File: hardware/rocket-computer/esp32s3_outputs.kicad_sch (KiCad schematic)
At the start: 40 parts, among them J5 Conn_01x04, SW3 R-667995, U11 GD5F2GQ5UEYIGR, U13 GD25Q128ESIG, U14 479480001, U15 ESP32-S3RH2, U29 TPS22810DRVR, Y1 ABS07-32.768KHZ-T, Y2 ECS-400-10-37B2-CKY-TR

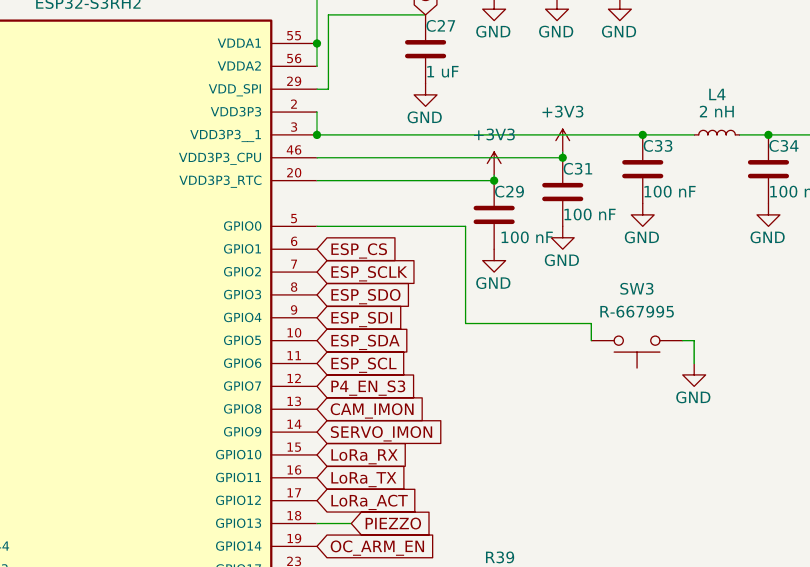
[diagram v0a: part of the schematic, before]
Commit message: hardware: I2S net names on both rocket computers; FC LED map and GPIO47/48 fixes (#987)
Renames the four inter-MCU link nets on both rocket computers to say what they
are — the link is I2S plus a sideband GPIO, and the names read as SPI:
ESP_SCLK -> ESP_I2S_BCLK, ESP_CS -> ESP_I2S_WS, ESP_SDO -> ESP_I2S_SD,
ESP_SDI -> ESP_I2S_FSYNC. ESP_SCL/ESP_SDA keep their names. ESP_I2S_FSYNC is not
a peripheral signal: the master pulses it around each writeFrame() and the slave
reads it to resync. Boards fabbed before this carry the old labels; the GPIO
numbers are unchanged and board_v9.h records both.

Also fixes three defects a header-vs-netlist parity sweep found on the mini:

- BMP585_CS and ISM6HG256_INT were swapped on both mini headers. ESP-IDF pins
  GPIO47 = SPICLK_P and GPIO48 = SPICLK_N; the schematic puts BMP585_CS on pad
  36 (SPICLK_N) and ISM6HG256_INT1 on pad 37 (SPICLK_P), so the correct numbers
  are 48 and 47. As shipped the barometer chip select would never have asserted
  and the IMU interrupt line would have been driven as an output.
- The flight computer has two LEDs, not one: IND_1 -> R70 -> D10 red on GPIO38
  and IND_2 -> R71 -> D11 blue on GPIO45. board_m1.h named the blue one red,
  left the red one unclaimed, and cited parts that do not exist. main.cpp drives
  BLUE_LED_PIN with no >= 0 guard, so the mini passed (gpio_num_t)-1 every boot.
- Docs corrected for FC GPIO3 (it carries VBUCK_OK through the R137/R138
  divider) and for the flight computer's spare pads (GPIO43 alone).

Includes the mini layout pass: 214 footprints placed, the 22.5 x 69.5 mm outline
restored on Edge.Cuts, and the board re-synced from the schematic. It is placed
but not routed. Before that re-sync the board file lagged the schematic by two
reworks and kicad-cli pcb drc --schematic-parity did not flag it, because it
reconciles footprints rather than stale net strings.

Verified: netlist fingerprints diff to exactly the four renames with identical
node lists on both boards; co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
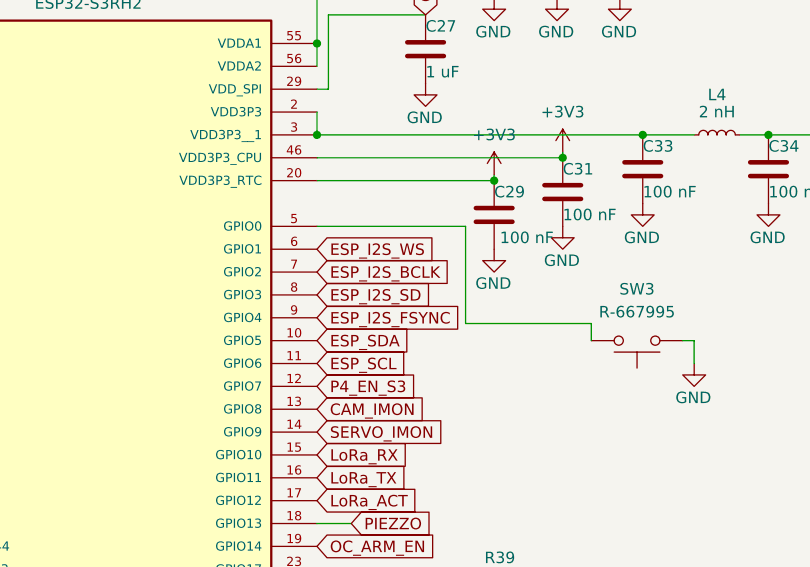
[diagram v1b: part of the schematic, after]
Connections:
- net ESP_CS renamed ESP_I2S_WS
- net ESP_SCLK renamed ESP_I2S_BCLK
- net ESP_SDI renamed ESP_I2S_FSYNC
- net ESP_SDO renamed ESP_I2S_SD
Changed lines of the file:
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@@
 		)
 	)
-	(global_label "ESP_CS"
+	(global_label "ESP_I2S_WS"
 		(shape input)
 		(at 212.725 53.34 0)
@@
 		)
 	)
-	(global_label "ESP_SCLK"
+	(global_label "ESP_I2S_BCLK"
 		(shape input)
 		(at 212.725 55.88 0)
@@
 		)
 	)
-	(global_label "ESP_SDO"
+	(global_label "ESP_I2S_SD"
 		(shape input)
 		(at 212.725 58.42 0)
@@
 		)
 	)
-	(global_label "ESP_SDI"
+	(global_label "ESP_I2S_FSYNC"
 		(shape input)
 		(at 212.725 60.96 0)

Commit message: hardware(V10): close out #664, #665 and #677 — the VDD_SPI 100 nF, the CHIP_PU rail-cycle analysis, and the harness cable rule (#1357)
Three items from the V9 pre-fab review list whose electrical content had
already landed; this closes what each still owed.

## #664 — C145 100 nF on OUT_VDD_SPI

The S3's VDD_SPI pin serves only the in-package PSRAM (the boot flash and
the NAND run from +3V3) and carried C27 1 uF alone; the design guide asks
for 1 uF + 0.1 uF at the pin and there was no pad for the second part.
C145 is drawn beside C27 on the same wire, split at (219.71, 27.305) with a
junction. Netlist: OUT_VDD_SPI = {C145.1, C27.1, U15.29}; C145.2 = GND.
bom.csv: 261 designators, 0 mismatches. WORKLIST M-4 and power-eco.md
Change 6 record the close-out. Placement at U15 pin 29 is the layout
pass's.

## #665 — CHIP_PU through a rail cycle

Both reset RCs are in copper on V9. The residual (the P4's C39 bleeding
into the QOD-collapsed rail at tau = 10 ms, so a rail re-raised inside
~14 ms would ramp with CHIP_PU high) is analysed in
v10-power-parity-2026-09-11.md section 6.2: the window is a coincidence
between C105's 0.45-0.94 s hold and the out computer's re-assert instant,
the pad clamp very likely collapses the node with the rail (inferred, not
specified), and a boot that misses t_STBL costs one extra rail cycle
because a P4 that never asserts P4_EN_HOLD gets its rail re-cycled by the
restore policy. The scope check that settles it is now on #1211. No part
change; the 100 nF that would shorten the window is the delay the design
guide asks for.

## #677 — mis-connection protection

Reverse battery is closed by Q11 with CR2 deleted; the PH-2-into-PH-4
mismate cannot happen since the battery moved to a JST-VH; the reversed
jumper is closed as a harness rule. New hardware/cables.md records the
straight "A"-suffix jumper part numbers (A04SR04SR30K51A, A05SR05SR30K51A),
the Digi-Key "Reversed" naming trap that cooked a radio on 2026-07-31, the
pad-1-to-pad-1 check, and 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
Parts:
- added C145: 100 nF, Capacitor_SMD:C_0402_1005Metric, symbol Device:C
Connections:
- net GND: now also C145.2
- net OUT_VDD_SPI: now also C145.1
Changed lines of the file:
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@@
 	(wire
 		(pts
-			(xy 213.995 27.305) (xy 224.79 27.305)
+			(xy 213.995 27.305) (xy 219.71 27.305)
 		)
 		(stroke
@@
 	(wire
 		(pts
+			(xy 219.71 27.305) (xy 224.79 27.305)
+		)
+		(stroke
+			(width 0)
+			(type default)
+		)
+	)
+	(junction
+		(at 219.71 27.305)
+		(diameter 0)
+		(color 0 0 0 0)
+	)
+	(wire
+		(pts
 			(xy 154.94 35.56) (xy 154.94 36.83)
 		)
@@
 			)
 		)
+	)
+	(symbol
+		(lib_id "Device:C")
+		(at 219.71 31.115 0)
+		(unit 1)
+		(body_style 1)
+		(exclude_from_sim no)
+		(in_bom yes)
+		(on_board yes)
+		(in_pos_files yes)
+		(dnp no)
+		(property "Reference" "C145"
+			(at 219.71 22.86 0)
+			(show_name no)
+			(do_not_autoplace no)
+			(effects
+				(font
+					(size 1.27 1.27)
+				)
+				(justify right)
+			)
+		)
+		(property "Value" "100 nF"
+			(at 219.71 25.4 0)
+			(show_name no)
+			(do_not_autoplace no)
+			(effects
+				(font
+					(size 1.27 1.27)
+				)
+				(justify right)
+			)
+		)
+		(property "Footprint" "Capacitor_SMD:C_0402_1005Metric"
+			(at 219.71 34.925 0)
+			(hide yes)
+			(show_name no)
+			(do_not_autoplace no)
+			(effects
+				(font
+					(size 1.27 1.27)
+				)
+			)
+		)
+		(property "Datasheet" ""
+			(at 219.71 31.115 0)
+			(hide yes)
+			(show_name no)
+			(do_not_autoplace no)
+			(effects
+				(font
+					(size 1.27 1.27)
+				)
+			)
+		)
+		(property "Description" "Unpolarized capacitor"
+			(at 219.71 31.115 0)
+			(hide yes)
+			(show_name no)
+			(do_not_autoplace no)
+			(effects
+				(font
+					(size 1.27 1.27)
+				)
+			)
+		)
+		(property "MPN" "CL05B104KO5NNNC"
+			(at 219.71 31.115 0)
+			(hide yes)
+			(show_name no)
+			(do_not_autoplace no)
+			(effects
+				(font
+					(size 1.27 1.27)
+				)
+			)
+		)
+		(property "Mfr" "Samsung"
+			(at 219.71 31.115 0)
+			(hide yes)
+			(show_name no)
+			(do_not_autoplace no)
+			(effects
+				(font
+					(size 1.27 1.27)
+				)
+			)
+		)
+		(pin "1"
+		)
+		(pin "2"
+		)
+		(instances
+			(project "rocket-computer"
+				(path "/ae61c2c4-72e9-4776-93ae-2e716b9dc70f/eab70588-b031-4461-adac-e038e88381cb"
+					(reference "C145")
+					(unit 1)
+				)
+			)
+		)
+	)
+	(symbol
+		(lib_id "power:GND")
+		(at 219.71 34.925 0)
+		(unit 1)
+		(body_style 1)
+		(exclude_from_sim no)
+		(in_bom yes)
+		(on_board yes)
+		(in_pos_files yes)
+		(dnp no)
+		(property "Reference" "#PWR0704"
+			(at 219.71 41.275 0)
+			(hide yes)
+			(show_name no)
+			(do_not_autoplace no)
+			(effects
+				(font
+					(size 1.27 1.27)
+				)
+			)
+		)
+		(property "Value" "GND"
+			(at 221.615 38.735 0)
+			(show_name no)
+			(do_not_autoplace no)
+			(effects
+				(font
+					(size 1.27 1.27)
+				)
+				(justify right)
+			)
+		)
+		(property "Footprint" ""
+			(at 219.71 34.925 0)
+			(hide yes)
+			(show_name no)
+			(do_not_autoplace no)
+			(effects
+				(font
+					(size 1.27 1.27)
+				)
+			)
+		)
+		(property "Datasheet" ""
+			(at 219.71 34.925 0)
+			(hide yes)
+			(show_name no)
+			(do_not_autoplace no)
+			(effects
+				(font
+					(size 1.27 1.27)
+				)
+			)
+		)
+		(property "Description" "Power symbol creates a global label with name \"GND\" , ground"
+			(at 219.71 34.925 0)
+			(hide yes)
+			(show_name no)
+			(do_not_autoplace no)
+			(effects
+				(font
+					(size 1.27 1.27)
+				)
+			)
+		)
+		(pin "1"
+		)
+		(instances
+			(project "rocket-computer"
+				(path "/ae61c2c4-72e9-4776-93ae-2e716b9dc70f/eab70588-b031-4461-adac-e038e88381cb"
+					(reference "#PWR0704")
+					(unit 1)
+				)
+			)
+		)

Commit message: hardware(V10): the #678 sweep — NRETRY to ground, LEDs at 1 k, H2 grounded, the missing bypasses, and the U9 pin-9 parity fix (#1360)
Schematic, library and BOM only; the board is untouched. Record:
hardware/rocket-computer/v10-power-parity-2026-09-11.md section 6.4.

## Owner decisions (2026-09-11)

- NRETRY to ground: C45 (1 uF, ~1800 retries, past the datasheet's last
  quantization bucket) deleted, U19 pin 11 tied to GND. With C46 2.2 nF
  still on RETRY_DLY the TPS25982 fault table reads "auto-retry
  indefinitely with finite delay" -- a finite count ends in latch-off,
  which a flight computer must never do.
- Status LEDs: R65, R66, R70 10 k -> 1 k (stocked line). ~1.5 mA green,
  ~1.3 mA red, ~0.4 mA blue instead of 0.05-0.15 mA.
- H2, the plated mounting ring 0.6 mm from the antenna body, on no net:
  H2 becomes Mechanical:MountingHole_Pad with pin 1 on GND. The other
  seven holes are unchanged; the pad's zone connection is the layout
  pass's.

## Simple adds from the same list

- C44 soft-start 390 pF -> 10 nF (the buck started in current limit into
  its output capacitance; ~5 ms now, datasheet class).
- R141 10 k pull-up on S3 GPIO0 to +3V3, on the wire to the boot button.
- C146 / C147 100 nF at the IMU and baro VDD pins (their nearest 100 nF
  was the magnetometer's at 3-4 mm), on V_MCU_SWTCH.
- C148 10 uF on the S3 RF supply net, converter side of L4 (the guide
  asks 10 uF per RF pin; there was only C33 100 nF).
- ISM6HG256_INT2: single-pin label replaced by a no-connect flag.
- U9 CSD16323Q3 symbol pin 9 renumbered 5 in Custom.kicad_sym and in the
  cached copies on this board and the mini: the shared TSON footprint
  numbers its drain tab as a second pad 5, so the symbol now matches it
  and the permanent "no pad for pin 9" parity warning is gone on both
  boards. Netlists unchanged.
- power-eco.md Change 2 pin table rewritten to the as-built designators
  and values (ITIMER/dVdt/NRETRY had drifted; the input clamp is gone).

Not changed, recorded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
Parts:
- added C148: 10 uF, Capacitor_SMD:C_0402_1005Metric, symbol Device:C
- added R141: 10 k, Resistor_SMD:R_0402_1005Metric, symbol Device:R_US
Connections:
- net +3V3: now also R141.2
- net GND: now also C148.2
- net at C33.1, L4.1, U15.2 (VDD3P3)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: now also C148.1
- net at SW3.2, U15.5 (GPIO0): now also R141.1

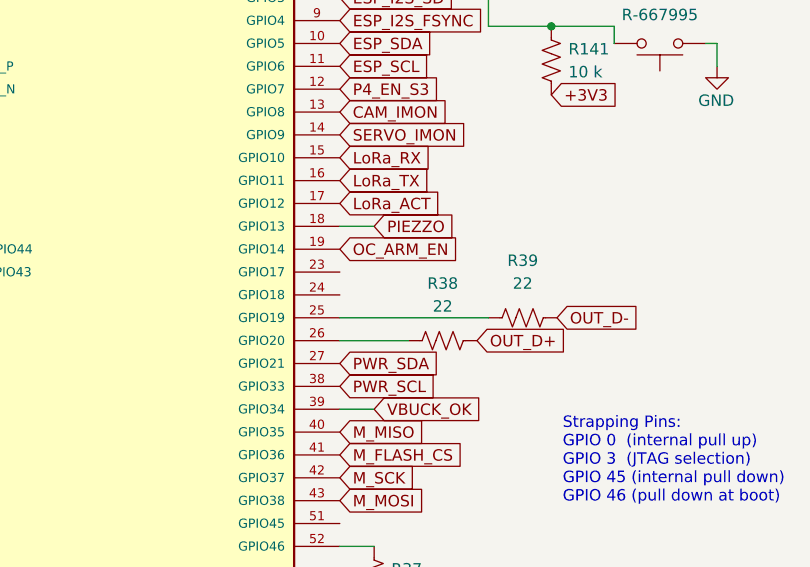
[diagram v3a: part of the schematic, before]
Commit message: hardware(V10): the eFuse's power-good and the INA230's alert reach the out computer (#721) (#1363)
PG_RAIL (U19 pin 13, open drain, R59 100 k to +3V3) onto S3 GPIO17 (pad 23); the INA230's ALERT (U23 pin 3, was unconnected) as a new INA_ALERT net onto S3 GPIO18 (pad 24) with R142 100 k to +3V3. Owner decisions 2026-09-11 on the recommendations: both signals, the out computer listens (always-on rail, pull-ups on the supercap-backed +3V3 so the pins read truthfully during a hold-up event), an external pull-up for the alert, U18's own PG skipped. This spends the S3's last two clean spare pins; the JTAG pads are the next reserve. Record: v10-power-parity-2026-09-11.md section 6.5.

Still open on #721 (firmware): board_v10.h with PG_RAIL_PIN = 17 / INA_ALERT_PIN = 18 (-1 on V9), the falling-edge latch on PG_RAIL into RTC memory written to the log as the reboot cause, and the INA230 alert threshold below the UVLO-equivalent current. Layout: two ~20 mm traces on the pass.

Verification: netlist vs main +R142; PG_RAIL gains U15.23; INA_ALERT = {U23.3, R142.2, U15.24}; R142.1 on +3V3; nothing else moves (277 comps / 241 nets). ERC --severity-all 1062 -> 1059: three pin_not_connected errors gone (pads 23/24, U23.3), no new category. bom.csv 82 rows / 265 designators / 0 mismatches. Docs gate clean.

Co-authored-by: Claude Fable 5.1 <noreply@anthropic.com>
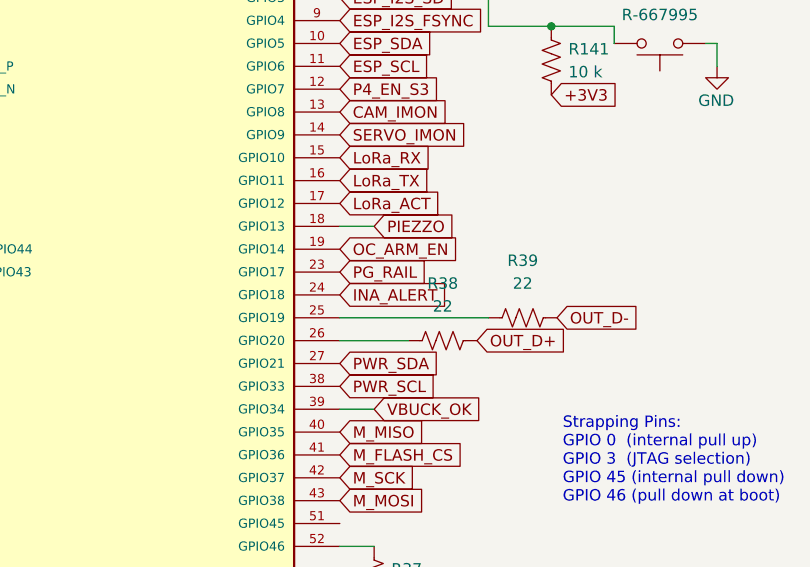
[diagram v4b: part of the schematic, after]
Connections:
- net PG_RAIL: now reaches U15.23 (GPIO17)
- net INA_ALERT: now reaches U15.24 (GPIO18)
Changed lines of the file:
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@@
+		)
+	)
+	(global_label "PG_RAIL"
+		(shape input)
+		(at 212.725 88.9 0)
+		(fields_autoplaced yes)
+		(effects
+			(font
+				(size 1.27 1.27)
+			)
+			(justify left)
+		)
+		(property "Intersheetrefs" "${INTERSHEET_REFS}"
+			(at 212.725 88.9 0)
+			(hide yes)
+			(show_name no)
+			(do_not_autoplace no)
+			(effects
+				(font
+					(size 1.27 1.27)
+				)
+				(justify left)
+			)
+		)
+	)
+	(global_label "INA_ALERT"
+		(shape input)
+		(at 212.725 91.44 0)
+		(fields_autoplaced yes)
+		(effects
+			(font
+				(size 1.27 1.27)
+			)
+			(justify left)
+		)
+		(property "Intersheetrefs" "${INTERSHEET_REFS}"
+			(at 212.725 91.44 0)
+			(hide yes)
+			(show_name no)
+			(do_not_autoplace no)
+			(effects
+				(font
+					(size 1.27 1.27)
+				)
+				(justify left)
+			)
 		)
 	)
